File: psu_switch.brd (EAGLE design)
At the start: 36.5 x 57.1 mm, 12 parts, among them K1 OMRON-G3MB-202P-SSR, T1 BC547

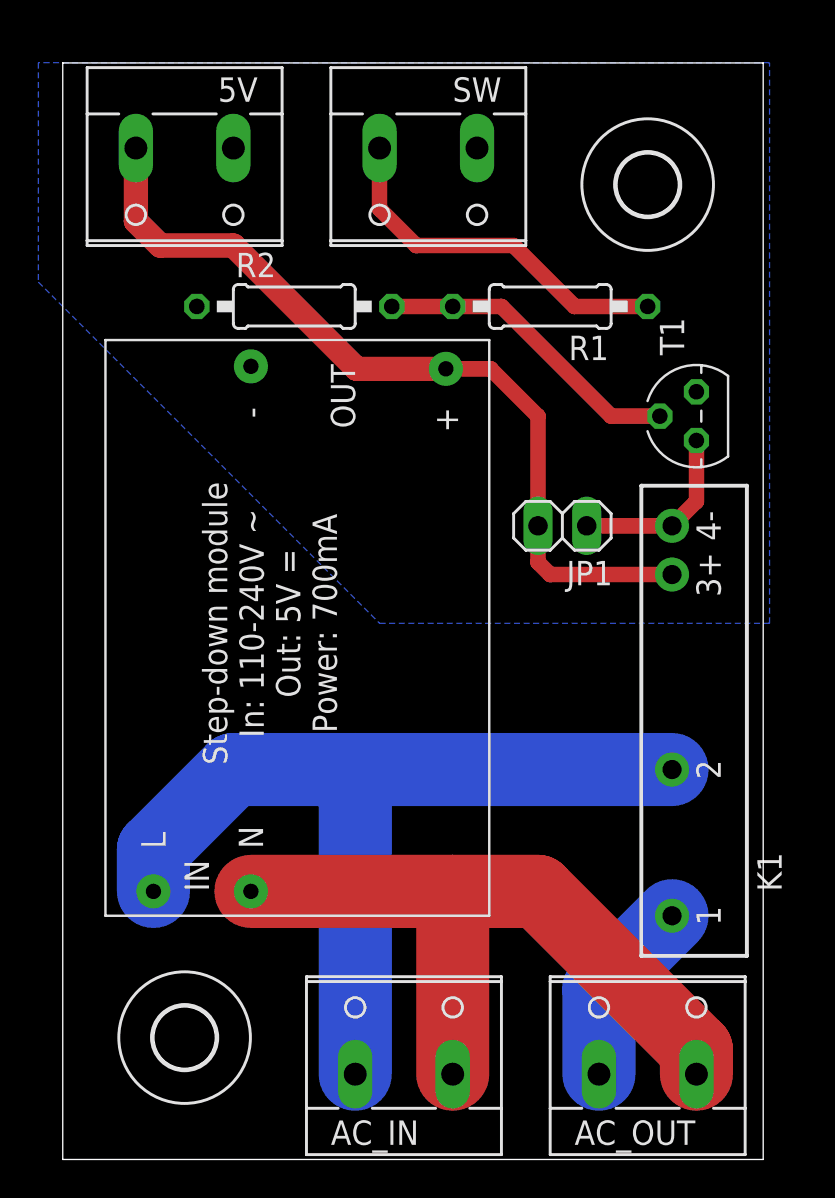
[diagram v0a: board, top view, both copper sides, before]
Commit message: Fix label and add GERBER files for PSU switch.
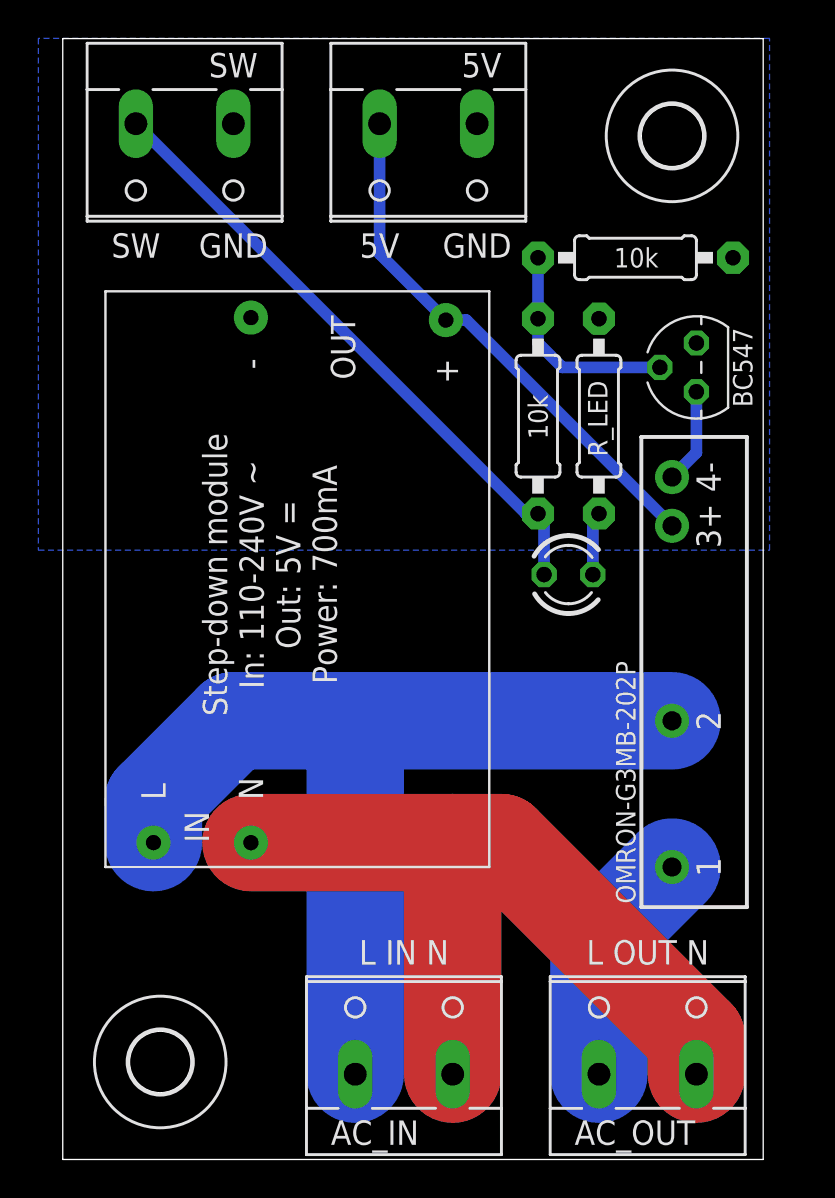
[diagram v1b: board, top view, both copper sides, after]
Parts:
- removed JP1: (no value), pinhead:1X02
- added LED1: (no value), led:LED3MM
- added R_LED: 10k, resistor:0207/10
- K1: value OMRON-G3MB-202P-SSR -> OMRON-G3MB-202P
- moved R2 18.0 mm to (29.8, 47.0), turned to 180 degrees
- moved 5V 12.8 mm to (19.1, 53.3)
- moved SW 12.8 mm to (6.35, 53.3)
- moved R1 5.75 mm to (24.8, 38.7), turned to 90 degrees
- moved H1 2.84 mm to (31.8, 53.3)
- moved U$1 2.54 mm to (22.2, 15.2)
- moved K1 2.54 mm to (31.8, 25.4)
- moved T1 2.54 mm to (33.0, 41.3)
- moved H2 1.80 mm to (5.08, 5.08)
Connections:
- net N$1 renamed L_OUT
- removed net 5V+: 5V.2, JP1.2, K1.3, U$1.5V+
- removed net N$2: R1.1, SW.2
- new net +5V: 5V.2, K1.3, U$1.5V+
- new net N$1: LED1.K, R_LED.2
- new net SW: LED1.A, R1.1, SW.2
- net GND: now also R_LED.1
- net N$5: no longer JP1.1
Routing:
- net 5V+: track 43.8 -> 0.00 mm
- net SW: track 0.00 -> 32.7 mm
- net +5V: track 0.00 -> 27.9 mm
- net N$2: track 19.2 -> 0.00 mm
- net SW+: track 16.3 -> 11.3 mm
- net N$5: track 9.42 -> 4.97 mm
- net N: track 37.4 -> 41.4 mm
- net N$1: track 0.00 -> 3.31 mm
- net L_OUT: track 9.83 -> 12.4 mm
- net L: track 46.8 -> 49.4 mm
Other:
- board size 36.5 x 57.1 mm -> 36.5 x 58.4 mm
- board text added: "5V"
- board text added: "GND"
- board text added: "L IN N"
- board text added: "L OUT N"
- board text added: "SW"
